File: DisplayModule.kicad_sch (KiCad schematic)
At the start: 11 parts, among them U1 74HC595

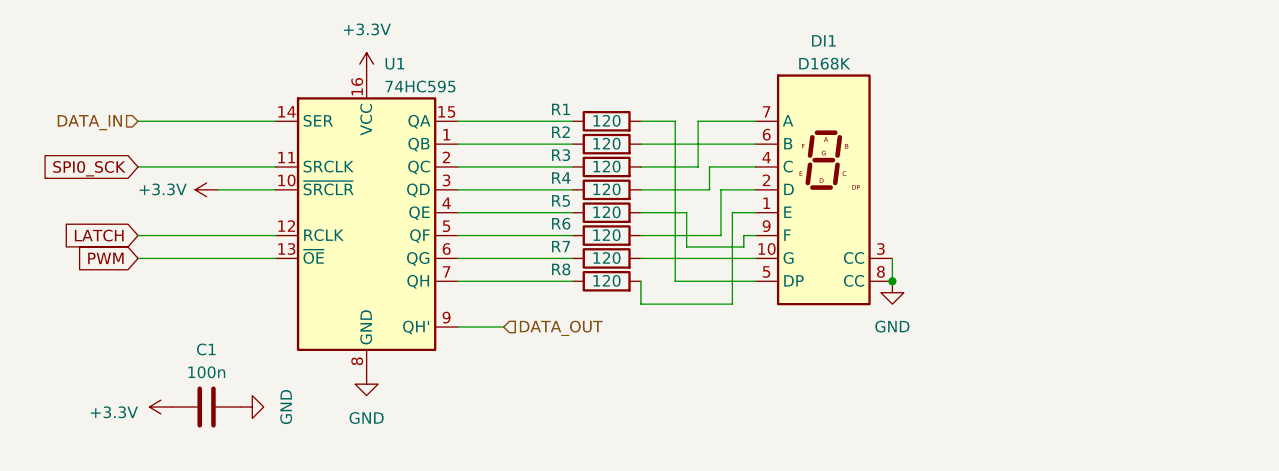
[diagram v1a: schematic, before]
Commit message: Consolidated Hardware on single board
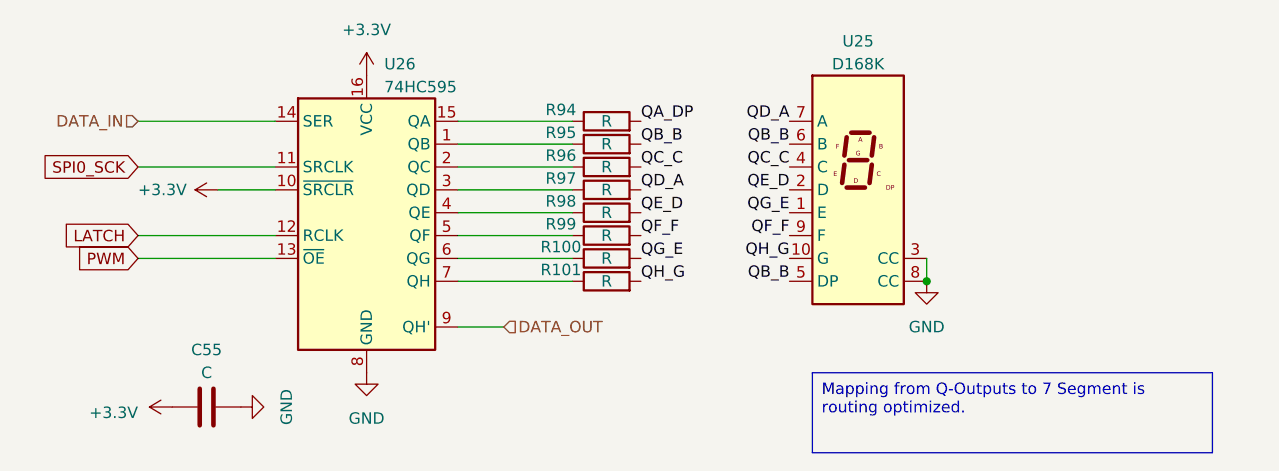
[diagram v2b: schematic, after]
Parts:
- C55: renamed from C1; value 100n -> C
- R100: renamed from R7; value 120 -> R
- R101: renamed from R8; value 120 -> R
- R94: renamed from R1; value 120 -> R
- R95: renamed from R2; value 120 -> R
- R96: renamed from R3; value 120 -> R
- R97: renamed from R4; value 120 -> R
- R98: renamed from R5; value 120 -> R
- R99: renamed from R6; value 120 -> R
- renumbered DI1 to U25, U1 to U26
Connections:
- net QB_B: now reaches R95.2, U25.6 (B)
- net QB_B: now also U25.5 (DP)
- net QC_C: now reaches U25.4 (C)
- net QC_C: now also R96.2; no longer R97.2
- net QG_E: now reaches U25.1 (E)
- net QG_E: now also R100.2; no longer R101.2
- net QH_G: now reaches U25.10 (G)
- net QH_G: now also R101.2; no longer R100.2
- net QE_D: now reaches U25.2 (D)
- net QE_D: now also R98.2; no longer R99.2
- net QA_DP: now reaches R94.2
- net QA_DP: no longer U25.5 (DP)
- net QD_A: now reaches U25.7 (A)
- net QD_A: now also R97.2; no longer R96.2
- net QF_F: now reaches U25.9 (F)
- net QF_F: now also R99.2; no longer R98.2
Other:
- company: (none) -> wirkbetrieb.net / Tom Eichhorn
- title: (none) -> Frankenstein Controller
- moved on the sheet: U25
